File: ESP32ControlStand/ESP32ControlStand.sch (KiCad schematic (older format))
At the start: 12 parts

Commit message: ESP32ControlStand Base I/O circuits.
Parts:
- added J?: I2C Display, ~, symbol CONN_6
- added J?: Button & LED Panel, ~, symbol CONN_5
- added J?: Light Switch, ~, symbol CONN_5
- added MOD?: I2C_DISPLAY, ~, symbol I2C_DISPLAY
- added P?: CONN_5, ~, symbol CONN_5
- added P?: CONN_4, ~, symbol CONN_6
- added SW?: LIGHT_SWITCH, ~, symbol LIGHT_SWITCH
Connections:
- net labels added: +3.3V, +Batt, GND, RST, SCL, SDA
- wire segments 32 -> 55
- no-connect marks 0 -> 1
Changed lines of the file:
@@
 LIBS:valves
 LIBS:encoder
+LIBS:rotatry_switch
+LIBS:i2c_display
+LIBS:MCP23xxx
+LIBS:tbd62x83a
+LIBS:esp32_devboards
 EELAYER 27 0
 EELAYER END
 $Descr A4 11693 8268
 encoding utf-8
-Sheet 1 1
+Sheet 1 2
 Title ""
-Date "1 oct 2019"
+Date "2 oct 2019"
 Rev ""
 Comp ""
@@
 Wire Wire Line
 	9350 4800 9250 4800
+$Comp
+L LIGHT_SWITCH SW?
+U 1 1 5D93E92F
+P 9900 1300
+F 0 "SW?" H 10250 950 60  0000 C CNN
+F 1 "LIGHT_SWITCH" H 10450 1800 60  0000 C CNN
+F 2 "~" H 9900 1300 60  0000 C CNN
+F 3 "~" H 9900 1300 60  0000 C CNN
+	1    9900 1300
+	-1   0    0    -1
+$EndComp
+$Comp
+L CONN_6 J?
+U 1 1 5D93E969
+P 8350 5450
+F 0 "J?" V 8300 5450 50  0000 C CNN
+F 1 "I2C Display" V 8400 5450 50  0000 C CNN
+F 2 "~" H 8350 5450 60  0000 C CNN
+F 3 "~" H 8350 5450 60  0000 C CNN
+	1    8350 5450
+	1    0    0    -1
+$EndComp
+$Comp
+L CONN_5 J?
+U 1 1 5D93E993
+P 8350 6450
+F 0 "J?" V 8300 6450 50  0000 C CNN
+F 1 "Button & LED Panel" V 8400 6450 50  0000 C CNN
+F 2 "~" H 8350 6450 60  0000 C CNN
+F 3 "~" H 8350 6450 60  0000 C CNN
+	1    8350 6450
+	1    0    0    -1
+$EndComp
+$Comp
+L CONN_5 J?
+U 1 1 5D93E9D1
+P 8400 1300
+F 0 "J?" V 8350 1300 50  0000 C CNN
+F 1 "Light Switch" V 8450 1300 50  0000 C CNN
+F 2 "~" H 8400 1300 60  0000 C CNN
+F 3 "~" H 8400 1300 60  0000 C CNN
+	1    8400 1300
+	1    0    0    -1
+$EndComp
+$Comp
+L CONN_5 P?
+U 1 1 5D93E9E0
+P 8850 1300
+F 0 "P?" V 8800 1300 50  0000 C CNN
+F 1 "CONN_5" V 8900 1300 50  0000 C CNN
+F 2 "~" H 8850 1300 60  0000 C CNN
+F 3 "~" H 8850 1300 60  0000 C CNN
+	1    8850 1300
+	-1   0    0    -1
+$EndComp
+Wire Wire Line
+	9250 1100 9350 1100
+Wire Wire Line
+	9350 1100 9350 1000
+Wire Wire Line
+	9350 1000 9600 1000
+Wire Wire Line
+	9250 1200 9400 1200
+Wire Wire Line
+	9400 1200 9400 1150
+Wire Wire Line
+	9400 1150 9600 1150
+Wire Wire Line
+	9250 1500 9450 1500
+Wire Wire Line
+	9450 1500 9450 1550
+Wire Wire Line
+	9450 1550 9600 1550
+Wire Wire Line
+	9250 1400 9600 1400
+Wire Wire Line
+	10350 1300 9250 1300
+$Sheet
+S 9150 6150 1250 650
+U 5D93EAD3
+F0 " Button and LED Panel" 50
+F1 "ButtonLEDPanel.sch" 50
+$EndSheet
+$Comp
+L CONN_6 P?
+U 1 1 5D93EADD
+P 8950 5450
+F 0 "P?" V 8900 5450 50  0000 C CNN
+F 1 "CONN_4" V 9000 5450 50  0000 C CNN
+F 2 "~" H 8950 5450 60  0000 C CNN
+F 3 "~" H 8950 5450 60  0000 C CNN
+	1    8950 5450
+	-1   0    0    -1
+$EndComp
+$Comp
+L I2C_DISPLAY MOD?
+U 1 1 5D93ED79
+P 9900 5450
+F 0 "MOD?" H 10050 5650 60  0000 C CNN
+F 1 "I2C_DISPLAY" H 10000 5350 60  0000 C CNN
+F 2 "~" H 9900 5450 60  0000 C CNN
+F 3 "~" H 9900 5450 60  0000 C CNN
+	1    9900 5450
+	1    0    0    -1
+$EndComp
+Wire Wire Line
+	9550 5200 9300 5200
+Wire Wire Line
+	9550 5300 9300 5300
+Wire Wire Line
+	9550 5400 9300 5400
+Wire Wire Line
+	9550 5500 9300 5500
+Wire Wire Line
+	9550 5600 9300 5600
+Wire Wire Line
+	9550 5700 9300 5700
+Text Label 7950 6250 2    60   ~ 0
++Batt
+Text Label 7950 6350 2    60   ~ 0
++3.3V
+Text Label 7950 6450 2    60   ~ 0
+GND
+Text Label 7950 6550 2    60   ~ 0
+SCL
+Text Label 7950 6650 2    60   ~ 0
+SDA
+Text Label 8000 5200 2    60   ~ 0
++Batt
+Text Label 8000 5400 2    60   ~ 0
+GND
+Text Label 8000 5500 2    60   ~ 0
+RST
+Text Label 8000 5600 2    60   ~ 0
+SCL
+Text Label 8000 5700 2    60   ~ 0
+SDA
+NoConn ~ 8000 5300
+$Comp
+L GND #PWR?
+U 1 1 5D94082C
+P 7850 1300
+F 0 "#PWR?" H 7850 1300 30  0001 C CNN
+F 1 "GND" H 7850 1230 30  0001 C CNN
+F 2 "" H 7850 1300 60  0000 C CNN
+F 3 "" H 7850 1300 60  0000 C CNN
+	1    7850 1300
+	0    1    1    0
+$EndComp
+Wire Wire Line
+	8000 1300 7850 1300
+$Comp
+L +3.3V #PWR?
+U 1 1 5D9408A0
+P 8000 2000
+F 0 "#PWR?" H 8000 1960 30  0001 C CNN
+F 1 "+3.3V" H 8000 2110 30  0000 C CNN
+F 2 "" H 8000 2000 60  0000 C CNN
+F 3 "" H 8000 2000 60  0000 C CNN
+	1    8000 2000
+	1    0    0    -1
+$EndComp
+$Comp
+L +3.3V #PWR?
+U 1 1 5D9408AF
+P 8000 2850
+F 0 "#PWR?" H 8000 2810 30  0001 C CNN
+F 1 "+3.3V" H 8000 2960 30  0000 C CNN
+F 2 "" H 8000 2850 60  0000 C CNN
+F 3 "" H 8000 2850 60  0000 C CNN
+	1    8000 2850
+	1    0    0    -1
+$EndComp
+$Comp
+L GND #PWR?
+U 1 1 5D9408BE
+P 8000 2450
+F 0 "#PWR?" H 8000 2450 30  0001 C CNN
+F 1 "GND" H 8000 2380 30  0001 C CNN
+F 2 "" H 8000 2450 60  0000 C CNN
+F 3 "" H 8000 2450 60  0000 C CNN
+	1    8000 2450
+	1    0    0    -1
+$EndComp
+$Comp
+L GND #PWR?
+U 1 1 5D9408CD
+P 8000 3250
+F 0 "#PWR?" H 8000 3250 30  0001 C CNN
+F 1 "GND" H 8000 3180 30  0001 C CNN
+F 2 "" H 8000 3250 60  0000 C CNN
+F 3 "" H 8000 3250 60  0000 C CNN
+	1    8000 3250
+	1    0    0    -1
+$EndComp
+$Comp
+L GND #PWR?
+U 1 1 5D9408DC
+P 7950 3950
+F 0 "#PWR?" H 7950 3950 30  0001 C CNN
+F 1 "GND" H 7950 3880 30  0001 C CNN
+F 2 "" H 7950 3950 60  0000 C CNN
+F 3 "" H 7950 3950 60  0000 C CNN
+	1    7950 3950
+	0    1    1    0
+$EndComp
+Wire Wire Line
+	8000 2000 8000 2150
+Wire Wire Line
+	8000 2350 8000 2450
+Wire Wire Line
+	8000 2850 8000 2950
+Wire Wire Line
+	8000 3150 8000 3250
+Wire Wire Line
+	8100 3950 7950 3950
 $EndSCHEMATC

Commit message: Completed first draft of PCBs for ESP32ControlStand.
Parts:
- added CON101: BARREL_JACK, ~, symbol BARREL_JACK
- added D101: Status, ~, symbol BI_LED
- added J101: Button & LED Panel, ~, symbol CONN_5
- added P101: CONN_8, ~, symbol CONN_8
- added P102: Misc buttons, bell, status LED, ~, symbol CONN_8
- added R101, R102: 220 Ohms, ~, symbol R
- added R103, R104, R105, R106: 100K Ohms, ~, symbol R
- added SW101: A, ~, symbol SW_PUSH_SMALL
- added SW102: B, ~, symbol SW_PUSH_SMALL
- added SW103: C, ~, symbol SW_PUSH_SMALL
- added SW104: D, ~, symbol SW_PUSH_SMALL
- added SW105: Bell, ~, symbol SW_PUSH_SMALL
- added U101: ADAFRUIT_POWERBOOST_500, ~, symbol ADAFRUIT_POWERBOOST_500
- added U102: TTGO-T1, ~, symbol TTGO-T1
- P108: renamed from P?; value CONN_4 -> CONN_6
- gave numbers to parts that had none: 18
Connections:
- net labels added: , +5V, Bell, Brake, Button_A, Button_B, Button_C, Button_D, CAN_RX, CAN_TX, Horn, L_Bright, L_Dim, L_Ditch, L_Off, MISO, MOSI, Reverser, SCLK, Status_G, Status_R, ThrottleA, ThrottleB
- net labels removed: +Batt
- wire segments 55 -> 114
- no-connect marks 1 -> 16

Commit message: Assorted updates to the PCB.
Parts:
- added J109: On-Off Switch, ~, symbol CONN_2
- EN101: Mouser Part Number 688-EC11E1820402 -> 706-25LB10-Q
- EN102: Mouser Part Number PEC12R-4117F-N0012 -> 652-PEC11R4325FN0012
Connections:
- net labels removed: 
- wire segments 114 -> 117
- no-connect marks 16 -> 15
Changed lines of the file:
@@
 F 2 "~" H 9900 4750 60  0000 C CNN
 F 3 "~" H 9900 4750 60  0000 C CNN
-F 4 "PEC12R-4117F-N0012" H 9900 4750 60  0001 C CNN "Mouser Part Number"
+F 4 "652-PEC11R4325FN0012" H 9900 4750 60  0001 C CNN "Mouser Part Number"
 	1    9900 4750
 	1    0    0    -1
@@
 F 2 "~" H 9900 3900 60  0000 C CNN
 F 3 "~" H 9900 3900 60  0000 C CNN
-F 4 "688-EC11E1820402" H 9900 3900 60  0001 C CNN "Mouser Part Number"
+F 4 "706-25LB10-Q" H 9900 3900 60  0001 C CNN "Mouser Part Number"
 	1    9900 3900
 	1    0    0    -1
@@
 Wire Wire Line
 	9550 5700 9300 5700
-Text Label 7950 6250 2    60   ~ 0
 Text Label 7950 6550 2    60   ~ 0
 SCL
@@
 	-1   0    0    -1
 $EndComp
-Text Label 3700 6550 0    60   ~ 0
 Text Label 3700 6850 0    60   ~ 0
 SCL
@@
 NoConn ~ 5650 1750
 NoConn ~ 5450 1750
-NoConn ~ 5350 1750
 NoConn ~ 5150 1750
 NoConn ~ 4900 3800
@@
 	1550 1100 1550 900
 Connection ~ 1550 900
+$Comp
+L CONN_2 J109
+U 1 1 5D9627A7
+P 5750 2200
+F 0 "J109" V 5700 2200 40  0000 C CNN
+F 1 "On-Off Switch" V 5800 2200 40  0000 C CNN
+F 2 "~" H 5750 2200 60  0000 C CNN
+F 3 "~" H 5750 2200 60  0000 C CNN
+	1    5750 2200
+	1    0    0    -1
+$EndComp
+Wire Wire Line
+	5350 1750 5350 2300
+Wire Wire Line
+	5350 2300 5400 2300
+Wire Wire Line
+	5400 2100 5400 1800
+Connection ~ 5400 1800
 $EndSCHEMATC

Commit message: Continue 3D model, spec out horn and brake pots, noturn hole for reverser.
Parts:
- RV101, RV102: Mouser Part Number (none) -> 774-450T328F104A1A1
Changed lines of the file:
@@
 Sheet 1 5
 Title ""
-Date "3 oct 2019"
+Date "5 oct 2019"
 Rev ""
 Comp ""
@@
 F 2 "~" H 10000 3000 60  0000 C CNN
 F 3 "~" H 10000 3000 60  0000 C CNN
+F 4 "774-450T328F104A1A1" H 10000 3000 60  0001 C CNN "Mouser Part Number"
 	1    10000 3000
 	0    -1   -1   0
@@
 F 2 "~" H 10050 2300 60  0000 C CNN
 F 3 "~" H 10050 2300 60  0000 C CNN
+F 4 "774-450T328F104A1A1" H 10050 2300 60  0001 C CNN "Mouser Part Number"
 	1    10050 2300
 	0    -1   -1   0

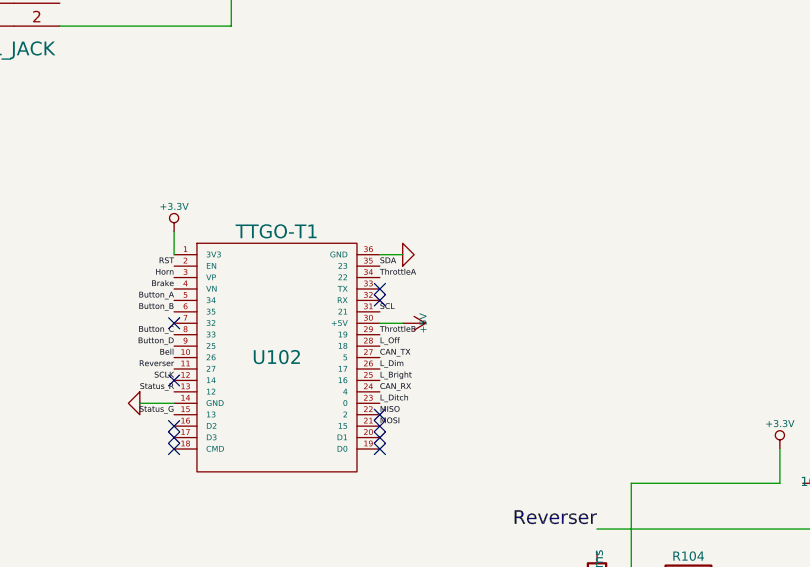
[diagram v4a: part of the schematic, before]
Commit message: Update circuit to use "Default" SDA/SDL.
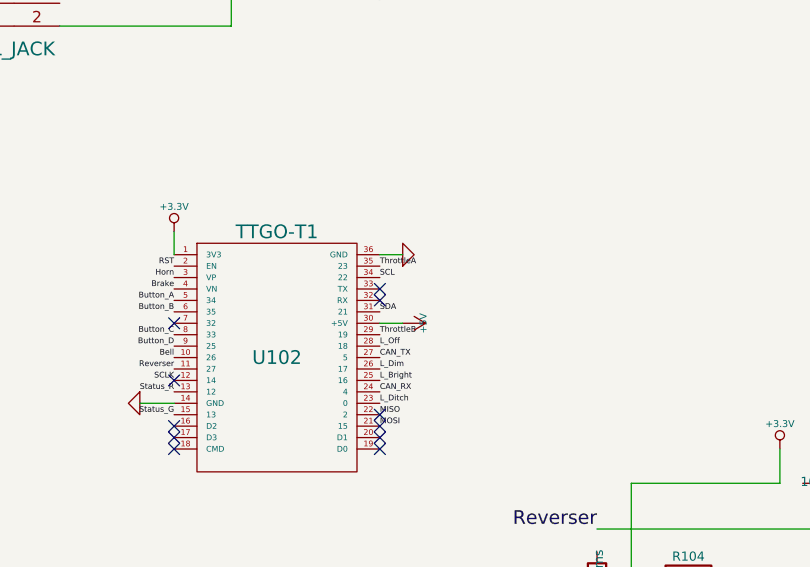
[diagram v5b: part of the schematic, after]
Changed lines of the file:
@@
 Sheet 1 5
 Title ""
-Date "5 oct 2019"
+Date "12 oct 2019"
 Rev ""
 Comp ""
@@
 Text Label 5800 4100 0    25   ~ 0
 CAN_RX
-Text Label 5800 3550 0    25   ~ 0
+Text Label 5800 3750 0    25   ~ 0
 SDA
-Text Label 5800 3750 0    25   ~ 0
+Text Label 5800 3600 0    25   ~ 0
 SCL
 Text Label 5800 4200 0    25   ~ 0
@@
 Text Label 8100 4050 2    60   ~ 0
 ThrottleB
-Text Label 5800 3600 0    25   ~ 0
+Text Label 5800 3550 0    25   ~ 0
 ThrottleA
 Text Label 5800 3850 0    25   ~ 0

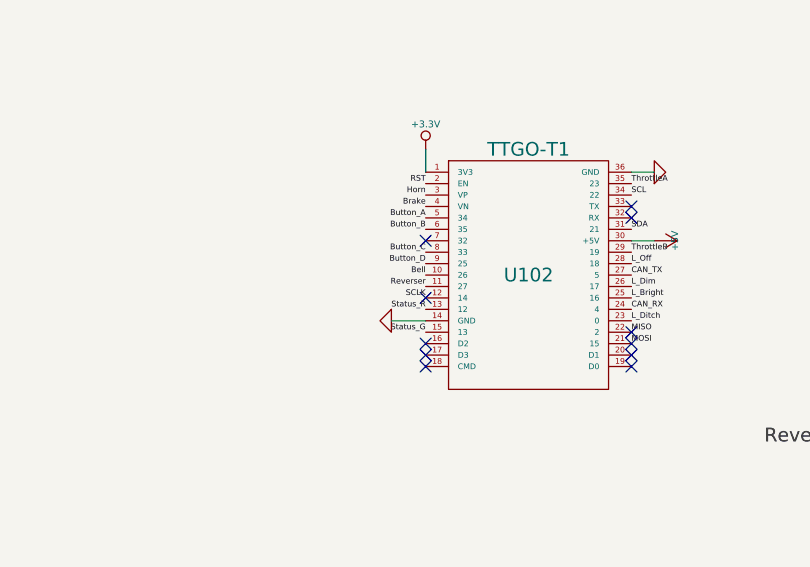
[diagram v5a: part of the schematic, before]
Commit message: Fix I/O conflict (Status_G).
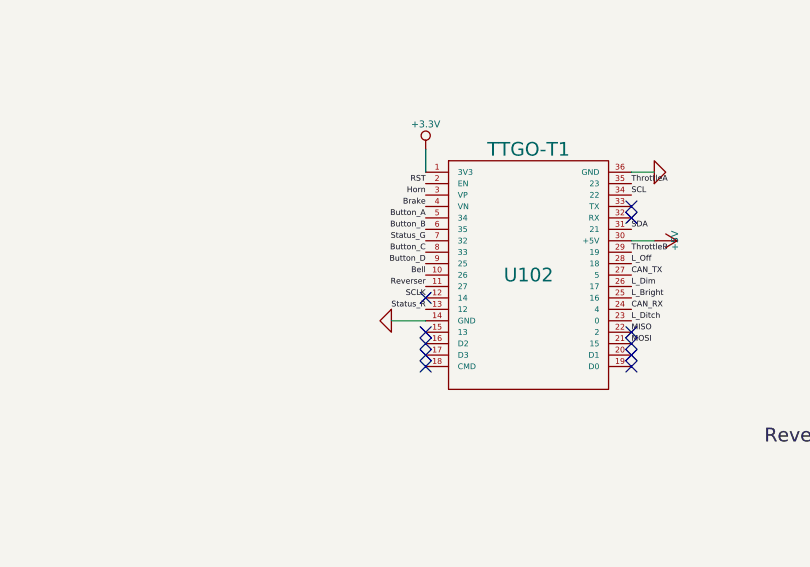
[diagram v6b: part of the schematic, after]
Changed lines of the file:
@@
 Text Label 4900 4100 2    25   ~ 0
 Status_R
-Text Label 4900 4200 2    25   ~ 0
+Text Label 4900 3800 2    25   ~ 0
 Status_G
 NoConn ~ 5650 1750
 NoConn ~ 5450 1750
 NoConn ~ 5150 1750
-NoConn ~ 4900 3800
 NoConn ~ 4900 4250
 NoConn ~ 4900 4300
@@
 	5400 2100 5400 1800
 Connection ~ 5400 1800
+NoConn ~ 4900 4200
 $EndSCHEMATC

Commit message: Continue FreeCAD work
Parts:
- MOD101: symbol I2C_DISPLAY -> I2C_Display
- R101, R102, R103, R104, R105, R106: symbol R -> R-RESCUE-ESP32ControlStand
- RV101, RV102: symbol POT -> POT-RESCUE-ESP32ControlStand
- SW106: symbol LIGHT_SWITCH -> Light_Switch
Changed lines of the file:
@@
 EESchema Schematic File Version 2
+LIBS:ESP32ControlStand-rescue
 LIBS:power
 LIBS:device
@@
 LIBS:memory
 LIBS:xilinx
-LIBS:special
 LIBS:microcontrollers
 LIBS:dsp
@@
 LIBS:adafruit_powerboost_500
 LIBS:ESP32ControlStand-cache
-EELAYER 27 0
+EELAYER 25 0
 EELAYER END
 $Descr A4 11693 8268
@@
 $EndComp
 $Comp
-L POT RV101
+L POT-RESCUE-ESP32ControlStand RV101
 U 1 1 5D93DC64
 P 10000 3000
@@
 $EndComp
 $Comp
-L POT RV102
+L POT-RESCUE-ESP32ControlStand RV102
 U 1 1 5D93DC73
 P 10050 2300
@@
 	9350 4800 9250 4800
 $Comp
-L LIGHT_SWITCH SW106
+L Light_Switch SW106
 U 1 1 5D93E92F
 P 9900 1300
@@
 $EndComp
 $Comp
-L I2C_DISPLAY MOD101
+L I2C_Display MOD101
 U 1 1 5D93ED79
 P 9900 5450
@@
 NoConn ~ 8000 5300
 $Comp
-L GND #PWR01
+L GND-RESCUE-ESP32ControlStand #PWR01
 U 1 1 5D94082C
 P 7850 1300
@@
 	8000 1300 7850 1300
 $Comp
-L +3.3V #PWR02
+L +3.3V-RESCUE-ESP32ControlStand #PWR02
 U 1 1 5D9408A0
 P 8000 2000
@@
 $EndComp
 $Comp
-L +3.3V #PWR03
+L +3.3V-RESCUE-ESP32ControlStand #PWR03
 U 1 1 5D9408AF
 P 8000 2850
@@
 $EndComp
 $Comp
-L GND #PWR04
+L GND-RESCUE-ESP32ControlStand #PWR04
 U 1 1 5D9408BE
 P 8000 2450
@@
 $EndComp
 $Comp
-L GND #PWR05
+L GND-RESCUE-ESP32ControlStand #PWR05
 U 1 1 5D9408CD
 P 8000 3250
@@
 $EndComp
 $Comp
-L GND #PWR06
+L GND-RESCUE-ESP32ControlStand #PWR06
 U 1 1 5D9408DC
 P 7950 3950
@@
 $EndComp
 $Comp
-L GND #PWR07
+L GND-RESCUE-ESP32ControlStand #PWR07
 U 1 1 5D94B400
 P 3000 1250
@@
 	3000 1250 2800 1250
 $Comp
-L R R101
+L R-RESCUE-ESP32ControlStand R101
 U 1 1 5D94B46B
 P 3200 1850
@@
 $EndComp
 $Comp
-L R R102
+L R-RESCUE-ESP32ControlStand R102
 U 1 1 5D94B47A
 P 3200 1950
@@
 	3700 6450 3700 6550
 $Comp
-L +3.3V #PWR011
+L +3.3V-RESCUE-ESP32ControlStand #PWR011
 U 1 1 5D94B319
 P 3900 6650
@@
 $EndComp
 $Comp
-L GND #PWR012
+L GND-RESCUE-ESP32ControlStand #PWR012
 U 1 1 5D94B32E
 P 3950 6750
@@
 	3700 6750 3950 6750
 $Comp
-L GND #PWR013
+L GND-RESCUE-ESP32ControlStand #PWR013
 U 1 1 5D94B6E3
 P 7750 6450
@@
 $EndComp
 $Comp
-L +3.3V #PWR014
+L +3.3V-RESCUE-ESP32ControlStand #PWR014
 U 1 1 5D94B6F8
 P 7800 6300
@@
 $EndComp
 $Comp
-L GND #PWR016
+L GND-RESCUE-ESP32ControlStand #PWR016
 U 1 1 5D94CB12
 P 5050 1850
@@
 $EndComp
 $Comp
-L +3.3V #PWR017
+L +3.3V-RESCUE-ESP32ControlStand #PWR017
 U 1 1 5D94E361
 P 4900 3400
@@
 $EndComp
 $Comp
-L GND #PWR019
+L GND-RESCUE-ESP32ControlStand #PWR019
 U 1 1 5D94E3AC
 P 5900 3500
@@
 $EndComp
 $Comp
-L GND #PWR020
+L GND-RESCUE-ESP32ControlStand #PWR020
 U 1 1 5D94E3CC
 P 4750 4150
@@
 ThrottleB
 $Comp
-L R R105
+L R-RESCUE-ESP32ControlStand R105
 U 1 1 5D951E1C
 P 7800 4500
@@
 $EndComp
 $Comp
-L R R106
+L R-RESCUE-ESP32ControlStand R106
 U 1 1 5D951ED9
 P 7800 4900
@@
 $EndComp
 $Comp
-L R R104
+L R-RESCUE-ESP32ControlStand R104
 U 1 1 5D951EF4
 P 7150 4900
@@
 $EndComp
 $Comp
-L R R103
+L R-RESCUE-ESP32ControlStand R103
 U 1 1 5D951F09
 P 6750 4950
@@
 	6900 4500 7550 4500
 $Comp
-L +3.3V #PWR021
+L +3.3V-RESCUE-ESP32ControlStand #PWR021
 U 1 1 5D9520F0
 P 7550 4350
@@
 	8050 4700 6750 4700
 $Comp
-L GND #PWR022
+L GND-RESCUE-ESP32ControlStand #PWR022
 U 1 1 5D9521F6
 P 6750 5300
@@
 Connection ~ 5150 1800
 $Comp
-L GND #PWR023
+L GND-RESCUE-ESP32ControlStand #PWR023
 U 1 1 5D9602D3
 P 1550 1100

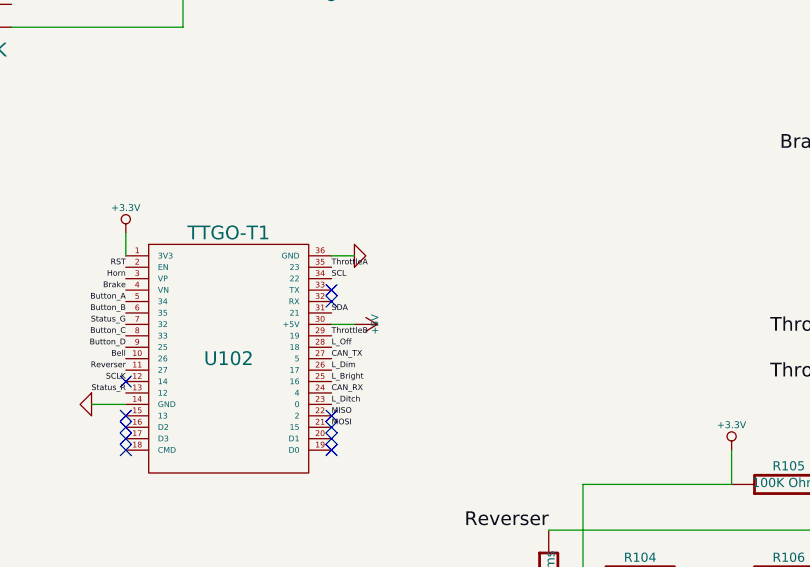
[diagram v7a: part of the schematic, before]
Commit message: Add I2C pullups.
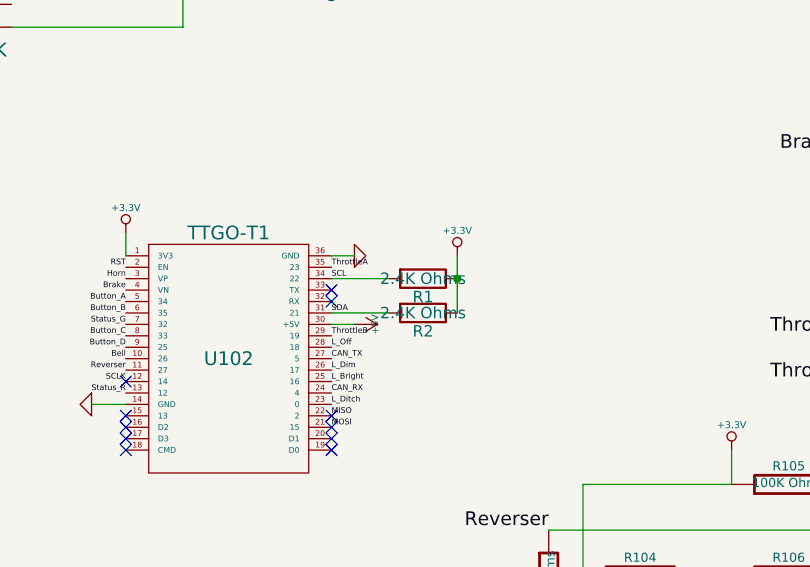
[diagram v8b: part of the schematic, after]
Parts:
- added R1, R2: 2.4K Ohms, Resistors_THT:R_Axial_DIN0207_L6.3mm_D2.5mm_P2.54mm_Vertical, symbol R
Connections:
- net +3.3V: now also R1.1, R2.1
- net SCL: now also R1.2
- net SDA: now also R2.2
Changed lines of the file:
@@
 EESchema Schematic File Version 2
-LIBS:ESP32ControlStand-rescue
 LIBS:power
 LIBS:device
@@
 Connection ~ 5400 1800
 NoConn ~ 4900 4200
+$Comp
+L R R1
+U 1 1 62002E5D
+P 6200 3600
+F 0 "R1" V 6280 3600 50  0000 C CNN
+F 1 "2.4K Ohms" V 6200 3600 50  0000 C CNN
+F 2 "Resistors_THT:R_Axial_DIN0207_L6.3mm_D2.5mm_P2.54mm_Vertical" V 6130 3600 50  0001 C CNN
+F 3 "" H 6200 3600 50  0001 C CNN
+	1    6200 3600
+	0    1    1    0
+$EndComp
+$Comp
+L R R2
+U 1 1 62002FC0
+P 6200 3750
+F 0 "R2" V 6280 3750 50  0000 C CNN
+F 1 "2.4K Ohms" V 6200 3750 50  0000 C CNN
+F 2 "Resistors_THT:R_Axial_DIN0207_L6.3mm_D2.5mm_P2.54mm_Vertical" V 6130 3750 50  0001 C CNN
+F 3 "" H 6200 3750 50  0001 C CNN
+	1    6200 3750
+	0    1    1    0
+$EndComp
+Wire Wire Line
+	6050 3600 5800 3600
+Wire Wire Line
+	6050 3750 5800 3750
+Wire Wire Line
+	6350 3500 6350 3750
+$Comp
+L +3.3V-RESCUE-ESP32ControlStand #PWR024
+U 1 1 62003529
+P 6350 3500
+F 0 "#PWR024" H 6350 3460 30  0001 C CNN
+F 1 "+3.3V" H 6350 3610 30  0000 C CNN
+F 2 "" H 6350 3500 60  0000 C CNN
+F 3 "" H 6350 3500 60  0000 C CNN
+	1    6350 3500
+	1    0    0    -1
+$EndComp
+Connection ~ 6350 3600
 $EndSCHEMATC
